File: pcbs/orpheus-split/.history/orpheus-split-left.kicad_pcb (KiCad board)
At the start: 2 copper layers, 138.1 x 88.1 mm, 46 parts, among them J1 AudioJack4, SW1 SW_Push, SW10 SW_Push, SW11 SW_Push, SW12 SW_Push, SW13 SW_Push, SW14 SW_Push, SW15 SW_Push, SW16 SW_Push, SW17 SW_Push, SW18 SW_Push, SW19 SW_Push, SW2 SW_Push, SW20 SW_Push, SW21 SW_Push, SW3 SW_Push, SW4 SW_Push, SW5 SW_Push, SW6 SW_Push, SW7 SW_Push, SW8 SW_Push, SW9 SW_Push

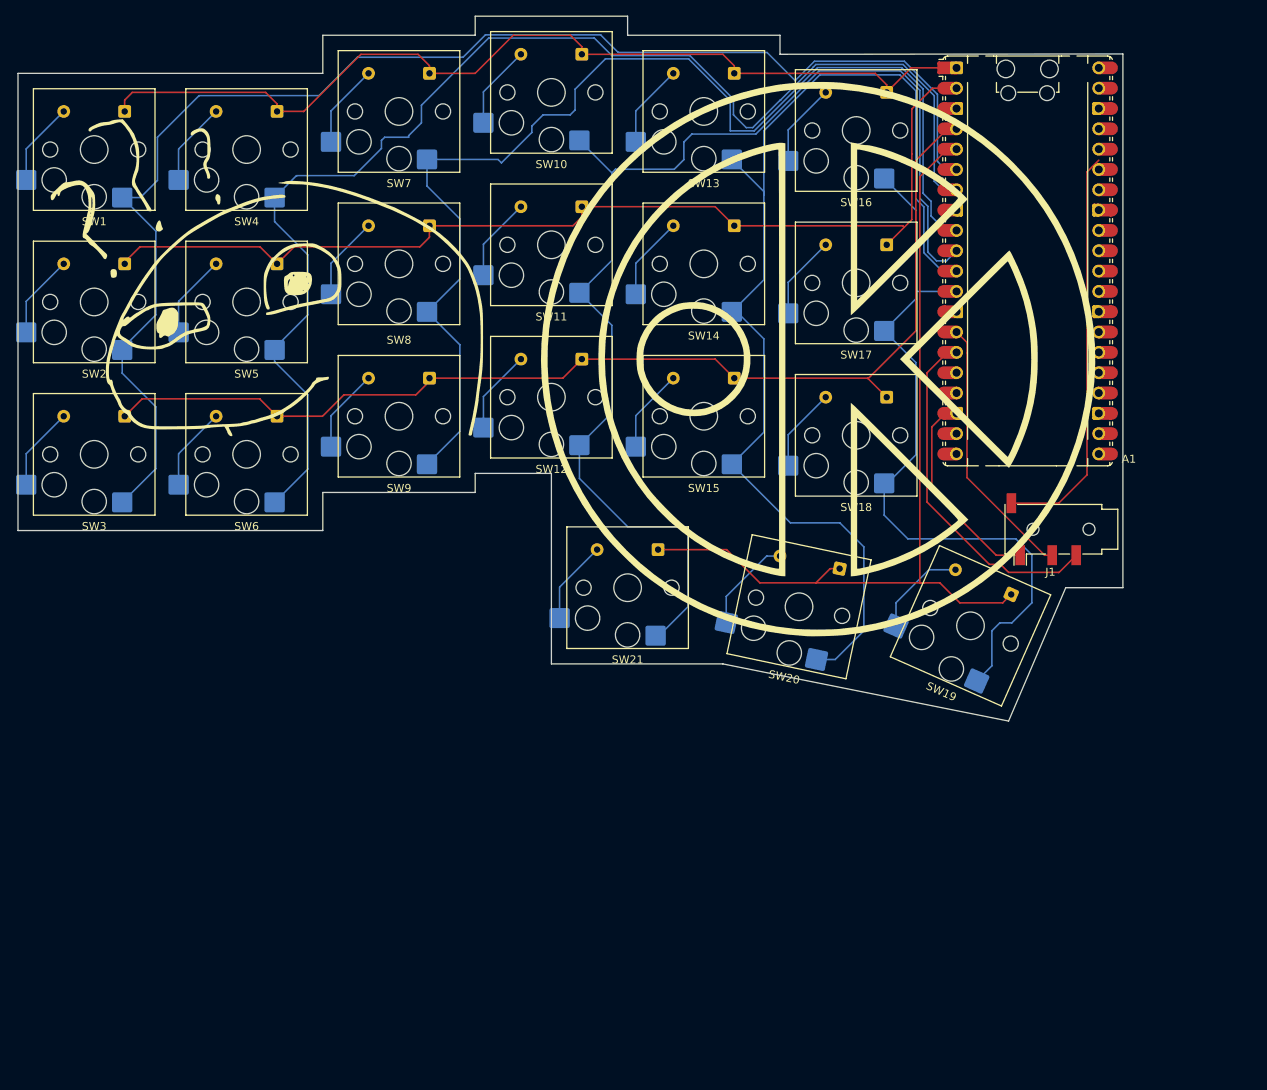
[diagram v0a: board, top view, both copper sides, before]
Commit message: finished the left pcb
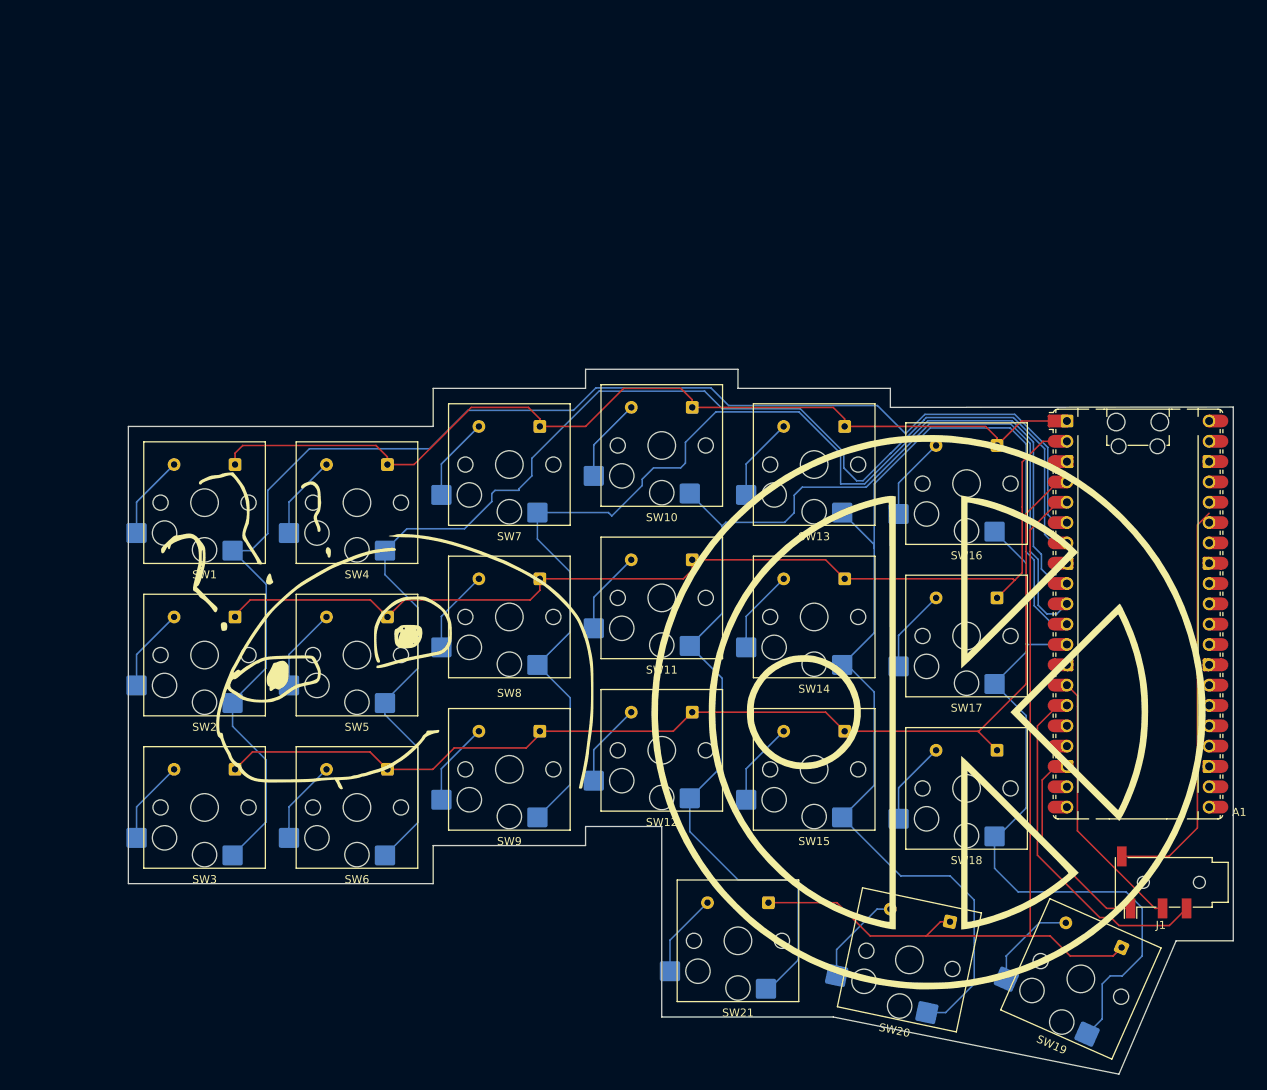
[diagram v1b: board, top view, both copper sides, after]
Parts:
- moved D20 46.2 mm to (171.3, 129.9)
- moved D1 46.2 mm to (81.9, 72.7)
- moved D11 46.2 mm to (139.1, 84.6)
- moved D12 46.2 mm to (139.1, 103.7)
- moved D13 46.2 mm to (158.1, 68.0)
- moved D14 46.2 mm to (158.1, 87.0)
- moved D18 46.2 mm to (177.2, 108.4)
- moved D19 46.2 mm to (192.7, 133.1)
- moved D2 46.2 mm to (81.9, 91.8)
- moved D21 46.2 mm to (148.6, 127.5)
- moved D3 46.2 mm to (81.9, 110.8)
- moved D4 46.2 mm to (101.0, 72.7)
- moved D5 46.2 mm to (101.0, 91.8)
- moved D6 46.2 mm to (101.0, 110.8)
- moved D7 46.2 mm to (120.0, 68.0)
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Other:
- outline, holes or cut-outs redrawn
